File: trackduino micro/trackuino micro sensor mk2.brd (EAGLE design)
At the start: 43.3 x 19 mm, 42 parts, among them IC2 74AHC1G125DBV, SW1 SPST_TACT-KMR2, U1 ATMEGA168MLF, Y1 16MHZ

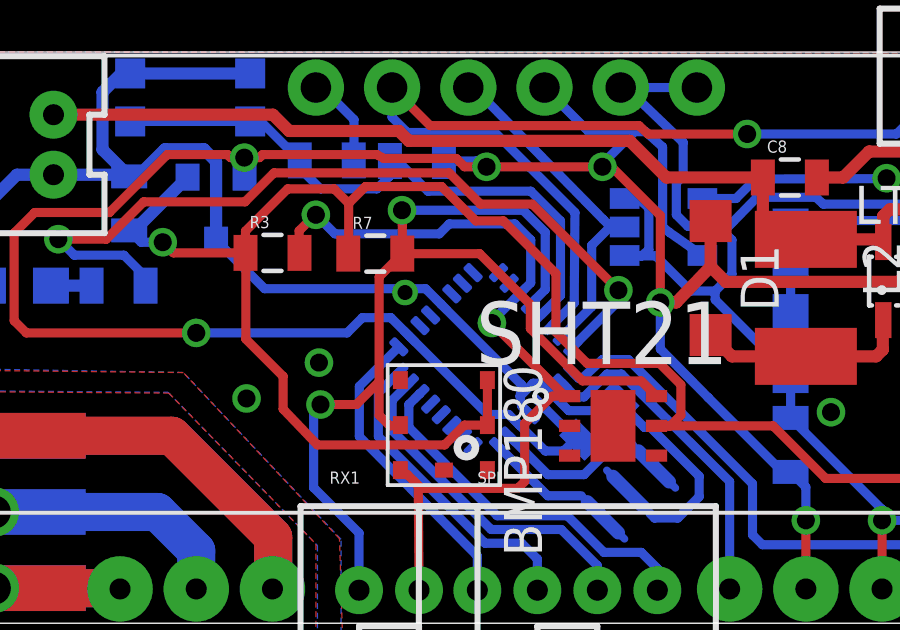
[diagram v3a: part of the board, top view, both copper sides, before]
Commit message: Removed Via From Under MCU
Removed a via from under the ATMEGA328P to prevent any potential
shorts.
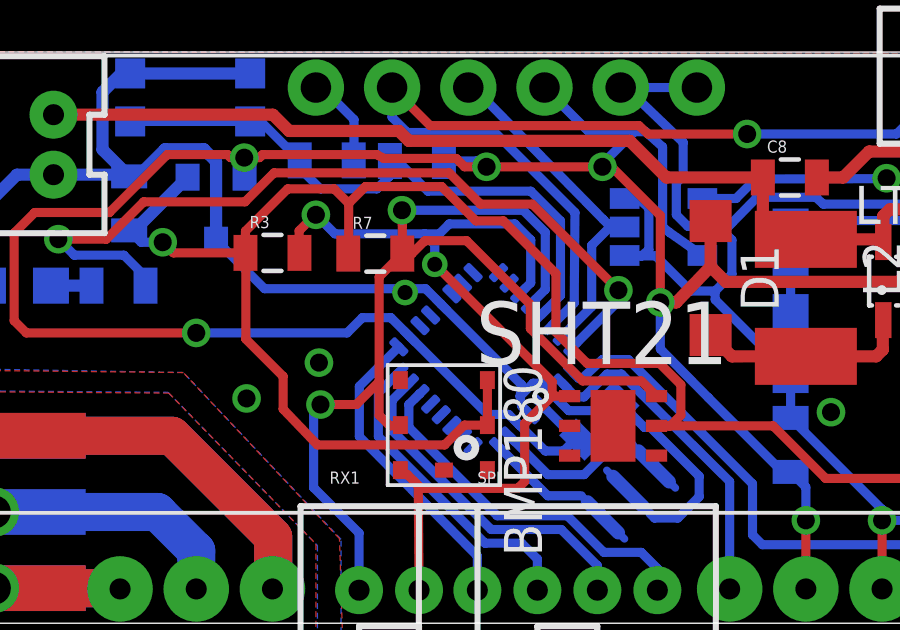
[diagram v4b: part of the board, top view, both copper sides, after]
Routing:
- net SDA: track 28.2 -> 30.5 mm
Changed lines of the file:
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@@
 <?xml version="1.0" encoding="utf-8"?>
 <!DOCTYPE eagle SYSTEM "eagle.dtd">
-<eagle version="7.2.0">
+<eagle version="7.1.0">
 <drawing>
 <settings>
@@
 <wire x1="18.3388" y1="13.3096" x2="16.1544" y2="13.3096" width="0.3048" layer="16"/>
 <wire x1="16.1544" y1="13.3096" x2="15.8242" y2="12.9794" width="0.3048" layer="16"/>
-<wire x1="15.8242" y1="12.9794" x2="12.3444" y2="12.9794" width="0.3048" layer="16"/>
+<wire x1="15.8242" y1="12.9794" x2="15.3416" y2="12.9794" width="0.3048" layer="16"/>
+<wire x1="15.3416" y1="12.9794" x2="12.3444" y2="12.9794" width="0.3048" layer="16"/>
 <wire x1="12.3444" y1="12.9794" x2="11.7094" y2="13.6144" width="0.3048" layer="16"/>
 <via x="11.7094" y="13.6144" extent="1-16" drill="0.6" shape="square"/>
@@
 <wire x1="19.5834" y1="7.5692" x2="20.1676" y2="7.5692" width="0.3048" layer="1"/>
 <wire x1="20.1676" y1="7.5692" x2="20.0152" y2="7.5692" width="0.3048" layer="1"/>
-<wire x1="20.0152" y1="7.5692" x2="17.5768" y2="10.0076" width="0.3048" layer="1"/>
-<via x="17.5768" y="10.0076" extent="1-16" drill="0.6"/>
-<wire x1="17.5768" y1="10.0076" x2="17.5768" y2="10.07765625" width="0.3048" layer="16"/>
-<wire x1="17.5768" y1="10.07765625" x2="18.504971875" y2="10.980428125" width="0.3048" layer="16"/>
 <contactref element="RX1" pad="2"/>
 <wire x1="15.1478" y1="1.101" x2="15.1224" y2="4.5814" width="0.3048" layer="1"/>
 <wire x1="15.1224" y1="4.5814" x2="14.9987" y2="4.7117" width="0.3048" layer="1"/>
+<wire x1="19.5834" y1="7.5692" x2="19.5834" y2="8.0518" width="0.3048" layer="1"/>
+<wire x1="19.5834" y1="8.0518" x2="15.6718" y2="11.9634" width="0.3048" layer="1"/>
+<via x="15.6718" y="11.9634" extent="1-16" drill="0.5" diameter="0.254"/>
+<wire x1="15.6718" y1="11.9634" x2="15.6718" y2="12.6238" width="0.3048" layer="16"/>
+<wire x1="15.6718" y1="12.6238" x2="15.3416" y2="12.9794" width="0.3048" layer="16"/>
 </signal>
 <signal name="SCL">
@@
 <wire x1="20.5994" y1="8.0772" x2="18.858525" y2="9.818075" width="0.3048" layer="1"/>
 <wire x1="18.858525" y1="9.818075" x2="18.858525" y2="10.626875" width="0.3048" layer="1"/>
-<wire x1="18.858525" y1="10.626875" x2="17.1664" y2="12.319" width="0.3048" layer="1"/>
-<wire x1="17.1664" y1="12.319" x2="14.5906" y2="12.319" width="0.3048" layer="1"/>
 <contactref element="RX1" pad="1"/>
 <wire x1="13.1478" y1="1.101" x2="13.1478" y2="3.0066" width="0.3048" layer="16"/>
@@
 <wire x1="11.8618" y1="7.2898" x2="13.0556" y2="7.2898" width="0.3048" layer="1"/>
 <wire x1="13.0556" y1="7.2898" x2="13.8176" y2="8.0518" width="0.3048" layer="1"/>
+<wire x1="14.5906" y1="12.319" x2="14.9098" y2="12.319" width="0.3048" layer="1"/>
+<wire x1="14.9098" y1="12.319" x2="15.3416" y2="12.7508" width="0.3048" layer="1"/>
+<wire x1="15.3416" y1="12.7508" x2="16.7346" y2="12.7508" width="0.3048" layer="1"/>
+<wire x1="16.7346" y1="12.7508" x2="18.858525" y2="10.626875" width="0.3048" layer="1"/>
 </signal>
 <signal name="15V">

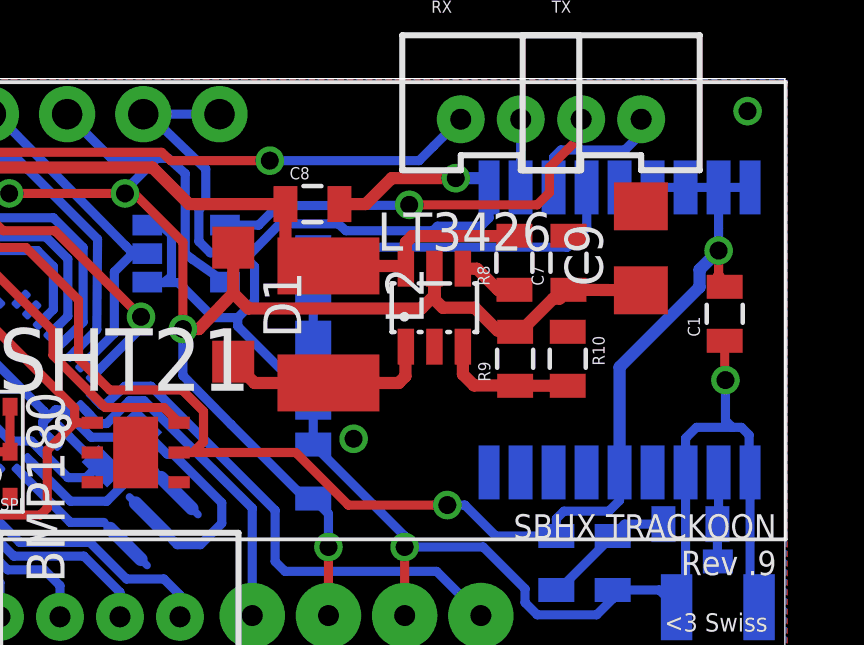
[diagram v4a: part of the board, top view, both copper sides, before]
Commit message: Standardized round via
Changed all via on production boards to round, and moved hidden via on
solar board out from under the atmega. Also fixed bom to specify
max-m8q gps.
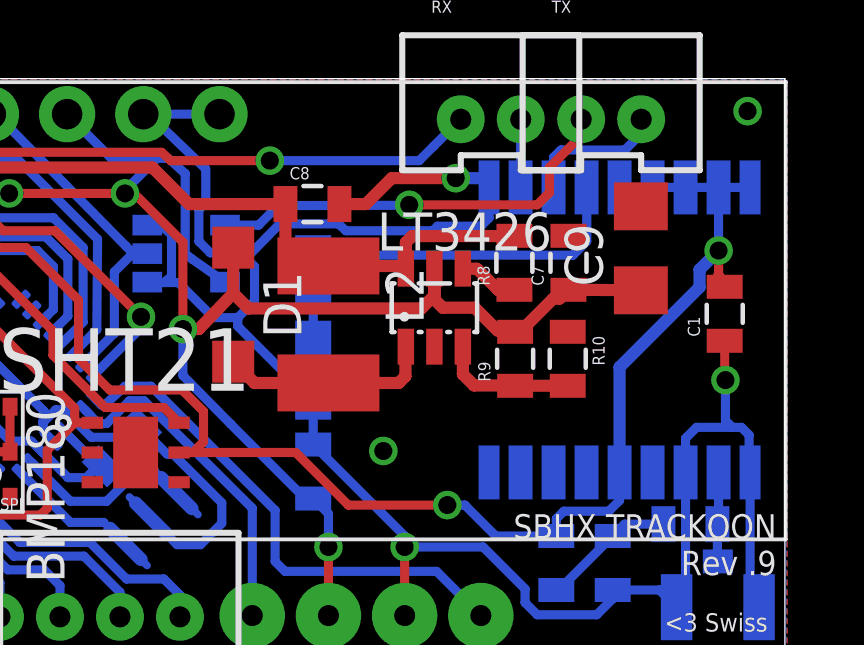
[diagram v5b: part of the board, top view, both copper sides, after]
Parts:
- renumbered LED1 to GPSLOCK
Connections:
- net N$2 renamed PPS

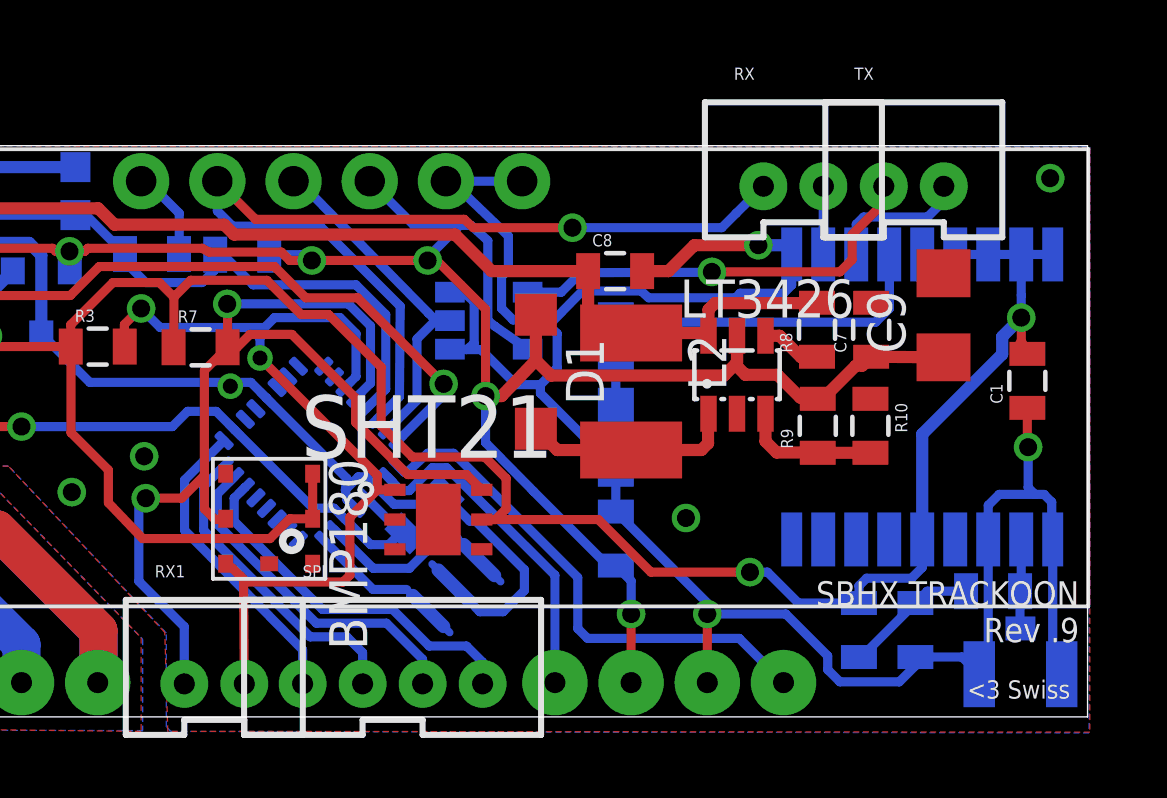
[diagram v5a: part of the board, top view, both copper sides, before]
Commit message: resolved DRC errors
Resolved DRC errors on both versions of the board.
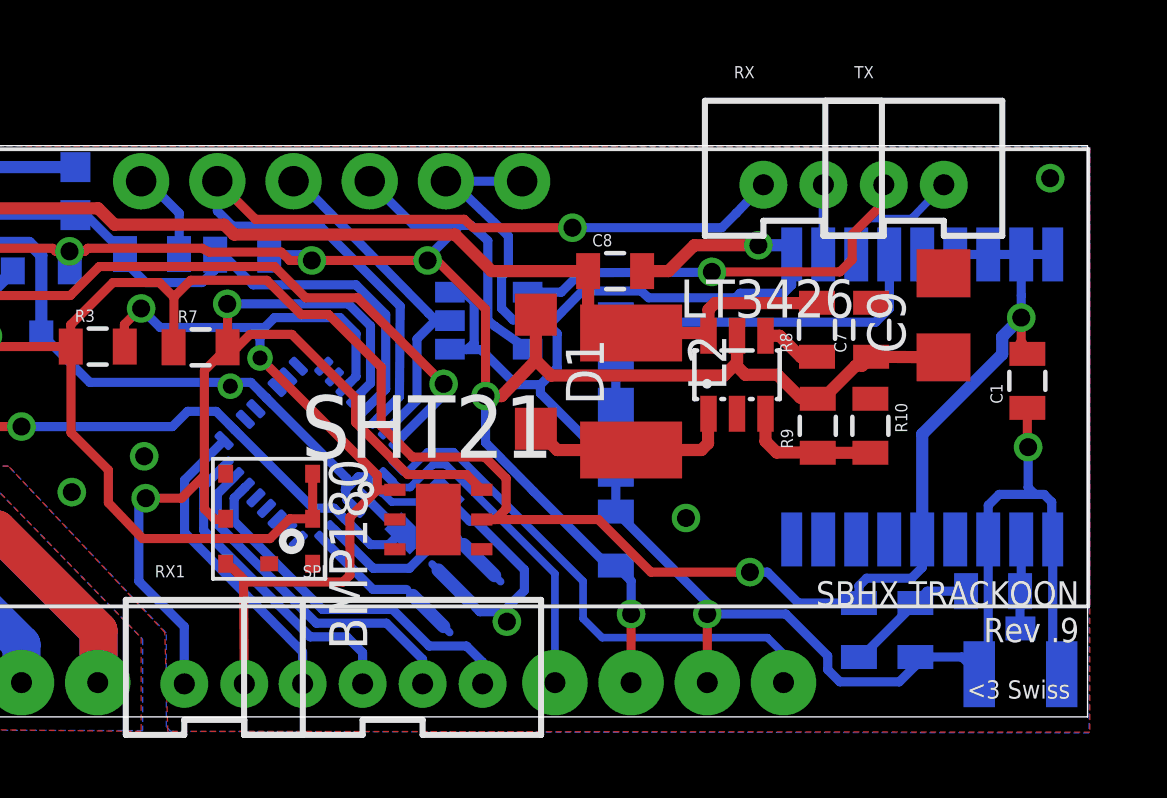
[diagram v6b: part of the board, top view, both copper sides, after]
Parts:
- moved RX 0.05 mm to (33.5, 18.3)
- moved TX 0.05 mm to (37.5, 18.3)
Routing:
- net GND: track 148.9 -> 148.8 mm, vias 9 -> 10
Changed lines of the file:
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@@
 <?xml version="1.0" encoding="utf-8"?>
 <!DOCTYPE eagle SYSTEM "eagle.dtd">
-<eagle version="7.1.0">
+<eagle version="7.2.0">
 <drawing>
 <settings>
@@
 <element name="R5" library="SparkFun-Resistors" package="0805" value="10k" x="15.077075" y="15.407278125" rot="MR180"/>
 <element name="C5" library="SparkFun-Capacitors" package="0805" value=".1uf" x="12.071159375" y="15.427575" rot="MR0"/>
-<element name="TX" library="SparkFun-Connectors" package="JST-2-PTH-VERT" value="TX" x="37.465" y="18.2372"/>
+<element name="TX" library="SparkFun-Connectors" package="JST-2-PTH-VERT" value="TX" x="37.465" y="18.288"/>
 <element name="SPI" library="SparkFun-Connectors" package="JST-4-PTH-VERT" value="" x="20.0914" y="1.651"/>
 <element name="FRAME1" library="SparkFun-Aesthetics" package="CREATIVE_COMMONS" value="FRAME-LETTER" x="14.3764" y="-8.1534"/>
@@
 <element name="R2" library="SparkFun-Resistors" package="0805" value="10ohm" x="35.6362" y="2.8956" rot="MR90"/>
 <element name="C6" library="SparkFun-Capacitors" package="0805" value="47pf" x="37.5158" y="2.8956" rot="MR270"/>
-<element name="RX" library="SparkFun-Connectors" package="JST-2-PTH-VERT" value="RX" x="33.4518" y="18.2372"/>
+<element name="RX" library="SparkFun-Connectors" package="JST-2-PTH-VERT" value="RX" x="33.4518" y="18.288"/>
 <element name="BMP180" library="SparkFun-Sensors" package="BMP180" value="BMP180" x="15.9766" y="6.604" rot="R270"/>
 <element name="R3" library="SparkFun-Resistors" package="0805" value="4.7k" x="10.2616" y="12.3444"/>
@@
 <wire x1="18.9484" y1="8.001" x2="19.221659375" y2="8.001" width="0.3048" layer="16"/>
 <wire x1="19.221659375" y1="8.001" x2="19.56563125" y2="7.657028125" width="0.3048" layer="16"/>
-<wire x1="19.56563125" y1="7.657028125" x2="20.136059375" y2="7.0866" width="0.3048" layer="16"/>
-<wire x1="20.136059375" y1="7.0866" x2="21.1328" y2="7.0866" width="0.3048" layer="16"/>
-<wire x1="21.1328" y1="7.0866" x2="21.43899375" y2="7.39279375" width="0.3048" layer="16"/>
-<wire x1="21.43899375" y1="7.39279375" x2="21.794596875" y2="7.39279375" width="0.3048" layer="16"/>
 <wire x1="15.888678125" y1="10.626875" x2="18.5674" y2="7.948153125" width="0.3048" layer="16"/>
 <wire x1="18.5674" y1="7.948153125" x2="18.5166" y2="7.5692" width="0.3048" layer="16"/>
@@
 <via x="11.811" y="8.6868" extent="1-16" drill="0.6"/>
 <via x="0.9906" y="1.1684" extent="1-16" drill="1.1" shape="square"/>
+<via x="23.9014" y="3.175" extent="1-16" drill="0.6"/>
+<wire x1="19.56563125" y1="7.657028125" x2="20.059859375" y2="7.1628" width="0.254" layer="16"/>
+<wire x1="20.059859375" y1="7.1628" x2="21.2344" y2="7.1628" width="0.254" layer="16"/>
+<wire x1="21.2344" y1="7.1628" x2="21.46439375" y2="7.39279375" width="0.254" layer="16"/>
+<wire x1="21.46439375" y1="7.39279375" x2="21.794596875" y2="7.39279375" width="0.254" layer="16"/>
 <wire x1="5.1816" y1="1.143" x2="5.207" y2="1.1684" width="0" layer="19" extent="1-1"/>
 <wire x1="9.398" y1="7.493" x2="6.9088" y2="6.2484" width="0" layer="19" extent="1-1"/>
-<wire x1="20.1676" y1="6.5786" x2="20.136059375" y2="7.0866" width="0" layer="19" extent="1-16"/>
 </signal>
 <signal name="VCC">
@@
 <contactref element="U1" pad="1"/>
 <contactref element="U$2" pad="TXD"/>
-<wire x1="20.272740625" y1="8.364134375" x2="20.483475" y2="8.1534" width="0.3048" layer="16"/>
-<wire x1="20.483475" y1="8.1534" x2="20.574" y2="8.1534" width="0.3048" layer="16"/>
-<wire x1="20.574" y1="8.1534" x2="21.2598" y2="8.7884" width="0.3048" layer="16"/>
-<wire x1="21.2598" y1="8.7884" x2="22.1234" y2="8.7884" width="0.3048" layer="16"/>
-<wire x1="22.1234" y1="8.7884" x2="26.2636" y2="4.6482" width="0.3048" layer="16"/>
-<wire x1="26.2636" y1="4.6482" x2="26.2636" y2="2.9464" width="0.3048" layer="16"/>
-<wire x1="26.2636" y1="2.9464" x2="26.5938" y2="2.6162" width="0.3048" layer="16"/>
-<wire x1="26.5938" y1="2.6162" x2="31.6484" y2="2.6162" width="0.3048" layer="16"/>
-<wire x1="31.6484" y1="2.6162" x2="33.1216" y2="1.143" width="0.3048" layer="16"/>
+<wire x1="20.272740625" y1="8.364134375" x2="20.483475" y2="8.1534" width="0.254" layer="16"/>
+<wire x1="20.483475" y1="8.1534" x2="20.574" y2="8.1534" width="0.254" layer="16"/>
+<wire x1="20.574" y1="8.1534" x2="21.2598" y2="8.8392" width="0.254" layer="16"/>
+<wire x1="21.2598" y1="8.8392" x2="22.1234" y2="8.8392" width="0.254" layer="16"/>
+<wire x1="22.1234" y1="8.8392" x2="26.4414" y2="4.5212" width="0.254" layer="16"/>
+<wire x1="26.4414" y1="4.5212" x2="26.4414" y2="3.2766" width="0.254" layer="16"/>
+<wire x1="26.4414" y1="3.2766" x2="27.0764" y2="2.6416" width="0.254" layer="16"/>
+<wire x1="27.0764" y1="2.6416" x2="32.5882" y2="2.6416" width="0.254" layer="16"/>
+<wire x1="32.5882" y1="2.6416" x2="33.1216" y2="2.1082" width="0.254" layer="16"/>
+<wire x1="33.1216" y1="2.1082" x2="33.1216" y2="1.143" width="0.254" layer="16"/>
 </signal>
 <signal name="TX">
 <contactref element="U$1" pad="2_TXD1"/>
 <contactref element="RX" pad="2"/>
-<wire x1="34.4518" y1="17.6872" x2="34.4424" y2="15.5192" width="0.3048" layer="16"/>
+<wire x1="34.4518" y1="17.738" x2="34.4424" y2="15.5192" width="0.3048" layer="16"/>
 <wire x1="34.4424" y1="15.5192" x2="34.4452" y2="15.4148" width="0.3048" layer="16"/>
 </signal>
@@
 <contactref element="U1" pad="2"/>
 <contactref element="U$2" pad="EN"/>
-<wire x1="19.9191875" y1="8.01058125" x2="20.36056875" y2="7.5438" width="0.3048" layer="16"/>
-<wire x1="20.36056875" y1="7.5438" x2="20.6502" y2="7.5438" width="0.3048" layer="16"/>
-<wire x1="20.6502" y1="7.5438" x2="21.4122" y2="8.3058" width="0.3048" layer="16"/>
-<wire x1="21.4122" y1="8.3058" x2="21.8948" y2="8.3058" width="0.3048" layer="16"/>
-<wire x1="21.8948" y1="8.3058" x2="25.5016" y2="4.7244" width="0.3048" layer="16"/>
-<wire x1="25.5016" y1="4.7244" x2="25.5016" y2="1.143" width="0.3048" layer="16"/>
+<wire x1="19.9191875" y1="8.01058125" x2="20.28436875" y2="7.6454" width="0.254" layer="16"/>
+<wire x1="20.28436875" y1="7.6454" x2="20.6756" y2="7.6454" width="0.254" layer="16"/>
+<wire x1="20.6756" y1="7.6454" x2="21.4376" y2="8.4074" width="0.254" layer="16"/>
+<wire x1="21.4376" y1="8.4074" x2="21.8694" y2="8.4074" width="0.254" layer="16"/>
+<wire x1="21.8694" y1="8.4074" x2="25.5016" y2="4.7752" width="0.254" layer="16"/>
+<wire x1="25.5016" y1="4.7752" x2="25.5016" y2="1.143" width="0.254" layer="16"/>
 </signal>
 <signal name="3V">
@@
 <contactref element="U$1" pad="3_RXD1"/>
 <contactref element="TX" pad="2"/>
-<wire x1="35.5452" y1="15.4148" x2="35.5452" y2="16.419" width="0.3048" layer="16"/>
-<wire x1="35.5452" y1="16.419" x2="35.7886" y2="16.6624" width="0.3048" layer="16"/>
-<wire x1="35.7886" y1="16.6624" x2="37.9222" y2="16.6624" width="0.3048" layer="16"/>
-<wire x1="37.9222" y1="16.6624" x2="38.4556" y2="17.1958" width="0.3048" layer="16"/>
-<wire x1="38.4556" y1="17.1958" x2="38.465" y2="17.6872" width="0.3048" layer="16"/>
+<wire x1="35.5452" y1="15.4148" x2="35.5452" y2="16.2158" width="0.254" layer="16"/>
+<wire x1="35.5452" y1="16.2158" x2="35.941" y2="16.6116" width="0.254" layer="16"/>
+<wire x1="35.941" y1="16.6116" x2="37.3894" y2="16.6116" width="0.254" layer="16"/>
+<wire x1="37.3894" y1="16.6116" x2="38.465" y2="17.738" width="0.254" layer="16"/>
 </signal>
 <signal name="DTR">
@@
 <wire x1="14.7574" y1="16.3576" x2="14.2494" y2="16.8656" width="0.3048" layer="16"/>
 <wire x1="14.2494" y1="16.8656" x2="14.2494" y2="17.8562" width="0.3048" layer="16"/>
-<wire x1="32.4518" y1="17.6872" x2="31.5468" y2="16.7894" width="0.3048" layer="16"/>
+<wire x1="32.4518" y1="17.738" x2="31.5468" y2="16.7894" width="0.3048" layer="16"/>
 <wire x1="31.5468" y1="16.7894" x2="31.0642" y2="16.3068" width="0.3048" layer="16"/>
 <wire x1="31.0642" y1="16.3068" x2="26.0858" y2="16.3068" width="0.3048" layer="16"/>
@@
 <contactref element="U1" pad="17"/>
 <contactref element="SPI" pad="1"/>
-<wire x1="17.0914" y1="1.101" x2="17.0914" y2="2.238" width="0.3048" layer="16"/>
-<wire x1="17.0914" y1="2.238" x2="13.1572" y2="6.223" width="0.3048" layer="16"/>
-<wire x1="13.1572" y1="6.223" x2="13.1572" y2="7.8954" width="0.3048" layer="16"/>
+<wire x1="17.0914" y1="1.101" x2="17.0914" y2="2.1618" width="0.3048" layer="16"/>
+<wire x1="17.0914" y1="2.1618" x2="13.1572" y2="6.1468" width="0.3048" layer="16"/>
+<wire x1="13.1572" y1="6.1468" x2="13.1572" y2="7.8954" width="0.3048" layer="16"/>
 <wire x1="13.1572" y1="7.8954" x2="14.4744625" y2="9.2126625" width="0.3048" layer="16"/>
 </signal>
@@
 <wire x1="35.4076" y1="15.24" x2="35.4076" y2="16.0782" width="0.3048" layer="1"/>
 <wire x1="35.4076" y1="16.0782" x2="36.4744" y2="17.145" width="0.3048" layer="1"/>
-<wire x1="36.4744" y1="17.145" x2="36.465" y2="17.6872" width="0.3048" layer="1"/>
+<wire x1="36.4744" y1="17.145" x2="36.465" y2="17.738" width="0.3048" layer="1"/>
 </signal>
 <signal name="VDDD">
